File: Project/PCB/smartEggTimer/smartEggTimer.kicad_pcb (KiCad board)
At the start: 2 copper layers, 72 x 72 mm, 65 parts, among them J1 Conn_01x05_Pin, J2 Conn_01x03_Pin, J3 Conn_01x03_Pin, J4 Conn_01x06_Pin, J5 Conn_01x02_Socket, J6 Conn_01x02_Socket, J7 Conn_01x03_Pin, J8 Conn_01x03_Pin, Q1 STP60NF06L, SW1 SW_Push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

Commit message: replace footprints with JLCs' footprints
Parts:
- SW2: footprint custom-parts:RotaryEncoder_Alps_EC12E_Vertical_H20mm_Mounting-Holes-GND -> custom-parts:SW-TH_EC12E24204A2
- U1: footprint Package_QFP:LQFP-64_10x10mm_P0.5mm -> custom-parts:LQFP-64_L10.0-W10.0-P0.50-LS12.0-BL
- U2: footprint Package_TO_SOT_SMD:SOT-223-3_TabPin2 -> custom-parts:SOT-223_L6.5-W3.5-P2.30-LS7.0-BR
- moved SW2 3.76 mm to (126.2, 100.0), turned to -90 degrees
- moved C7 0.34 mm to (89.5, 97.3)
- moved C3 0.28 mm to (95.0, 112.5)
- moved C2 0.17 mm to (83.7, 109.1)
- turned U1 to 180 degrees
- turned U2 to 180 degrees
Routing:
- net +3.3V: track 316.9 -> 319.7 mm
- net GND: track 63.1 -> 65.8 mm
- net /NRST: track 62.7 -> 64.3 mm
- net /USART3_TX: track 15.6 -> 16.5 mm
- net /JTAG_SWCLK: track 15.5 -> 16.4 mm
- net /Button_1: track 17.5 -> 18.4 mm
- net /Rotary Encoder b: track 60.3 -> 61.1 mm
- net /Rotary Encoder a: track 61.7 -> 62.5 mm
- net /I2C1_SCL: track 30.3 -> 31.1 mm
- net /BOOT0: track 3.41 -> 4.08 mm

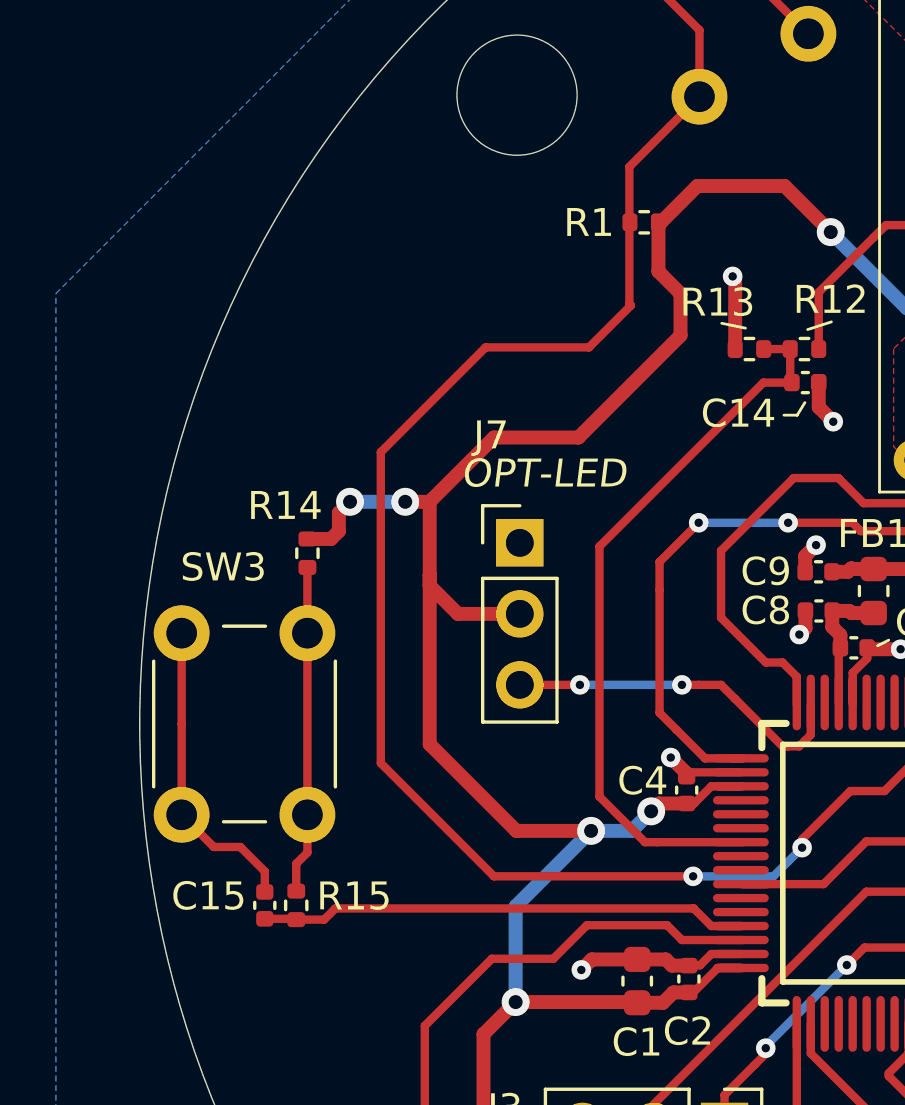
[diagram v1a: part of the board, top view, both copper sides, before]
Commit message: add logo
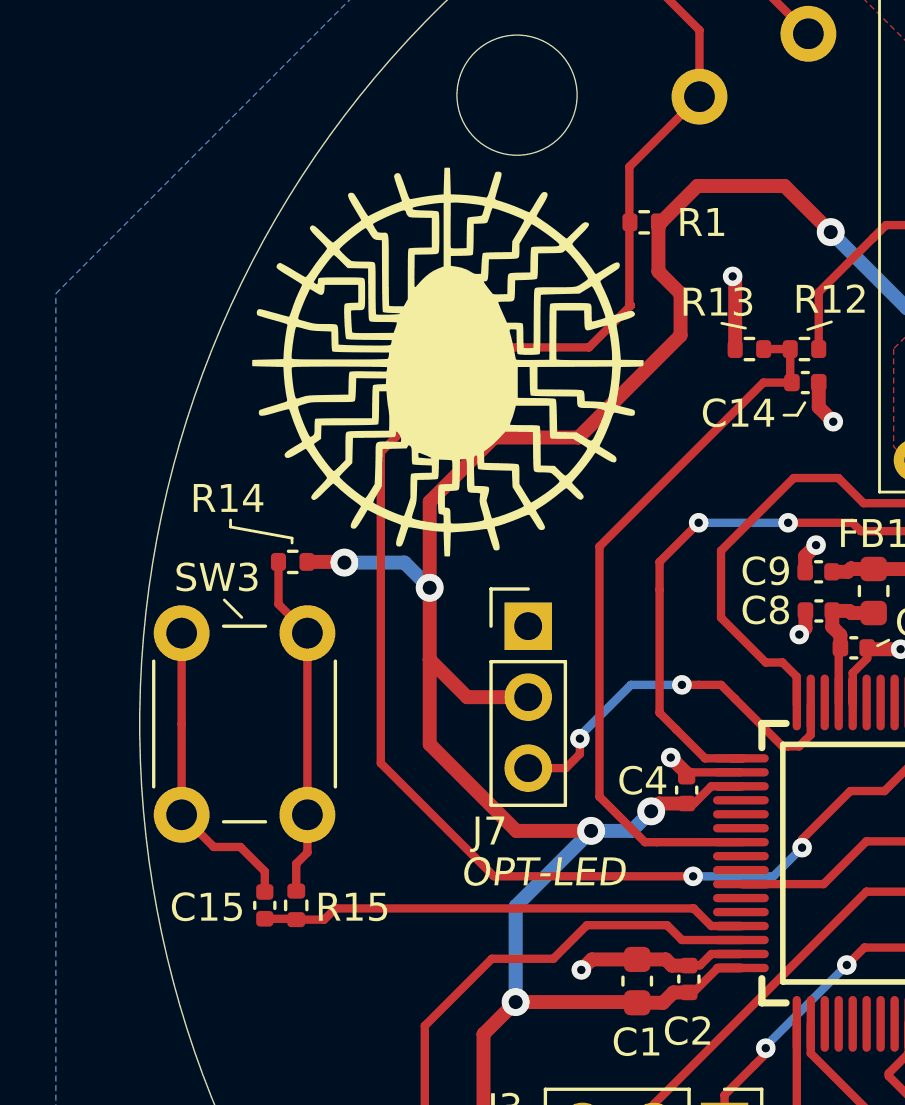
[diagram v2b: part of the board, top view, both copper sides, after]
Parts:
- added G***: LOGO, LOGO, F.Cu at (75.0, 87.0)
- moved J7 3.00 mm to (77.9, 96.5)
- moved R14 0.61 mm to (69.5, 94.2), turned to 0 degrees
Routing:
- net /LED: track 16.2 -> 13.9 mm
- net Net-(R14-Pad1): track 11.7 -> 12.4 mm
